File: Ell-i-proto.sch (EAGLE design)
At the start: 139 parts, among them J1 FTDI-SER-6, J10 PJ-102AX, J2 PWMH, J3 PWR, J4 PWML, J5 ANAL, J6 SPI, J7 COMM, J8 ANAH, J9 RJ45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

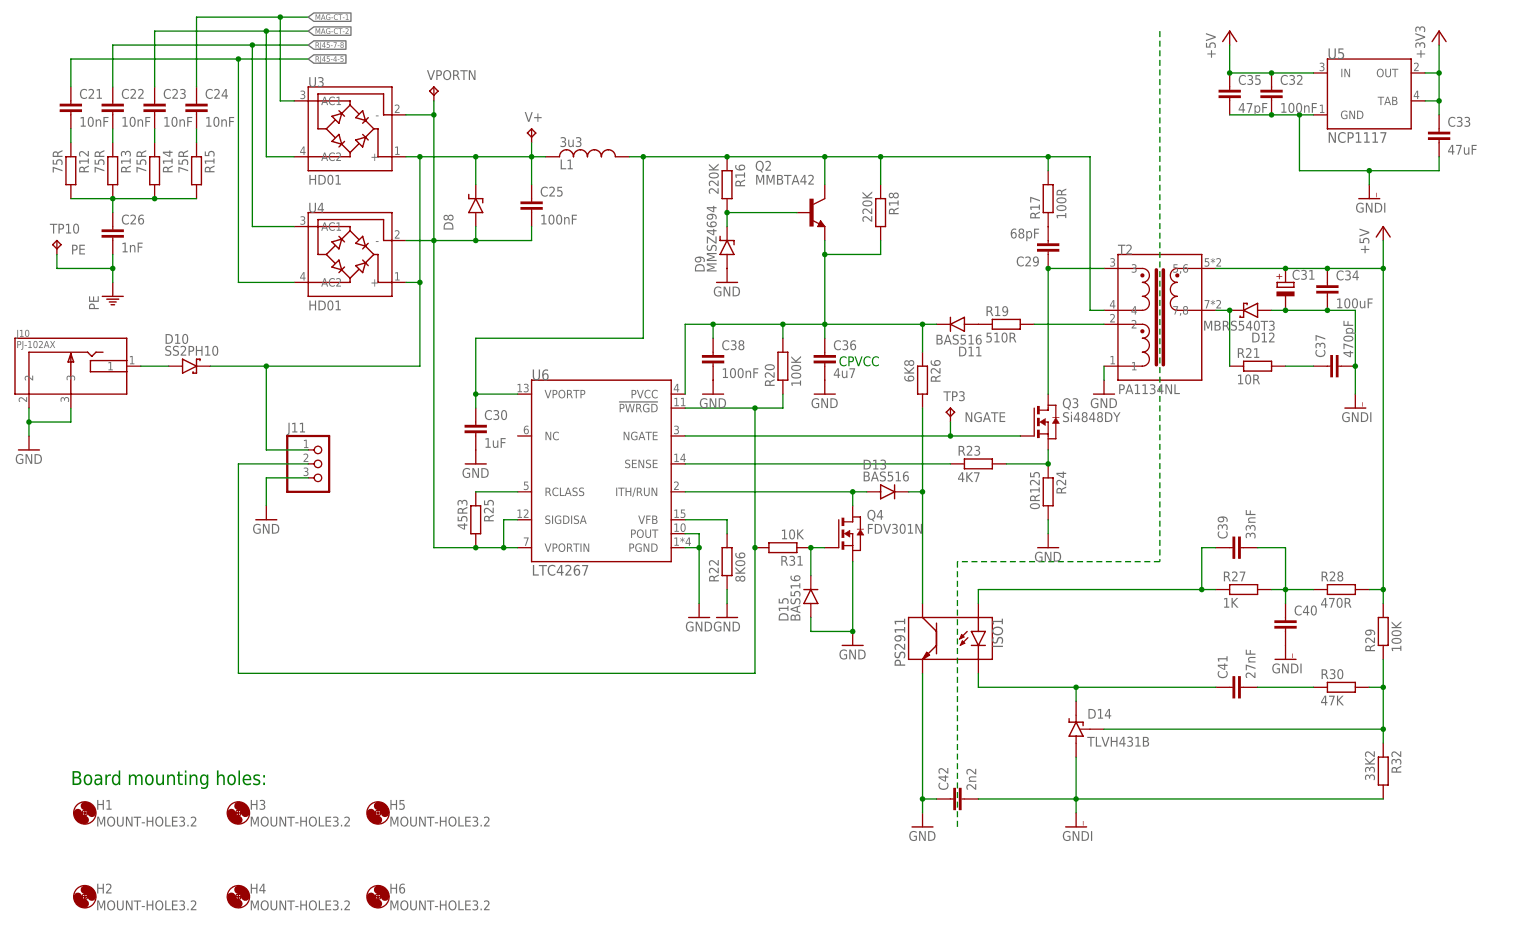
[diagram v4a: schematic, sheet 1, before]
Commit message: pushbutton and power LED to the right edge, some more drafting
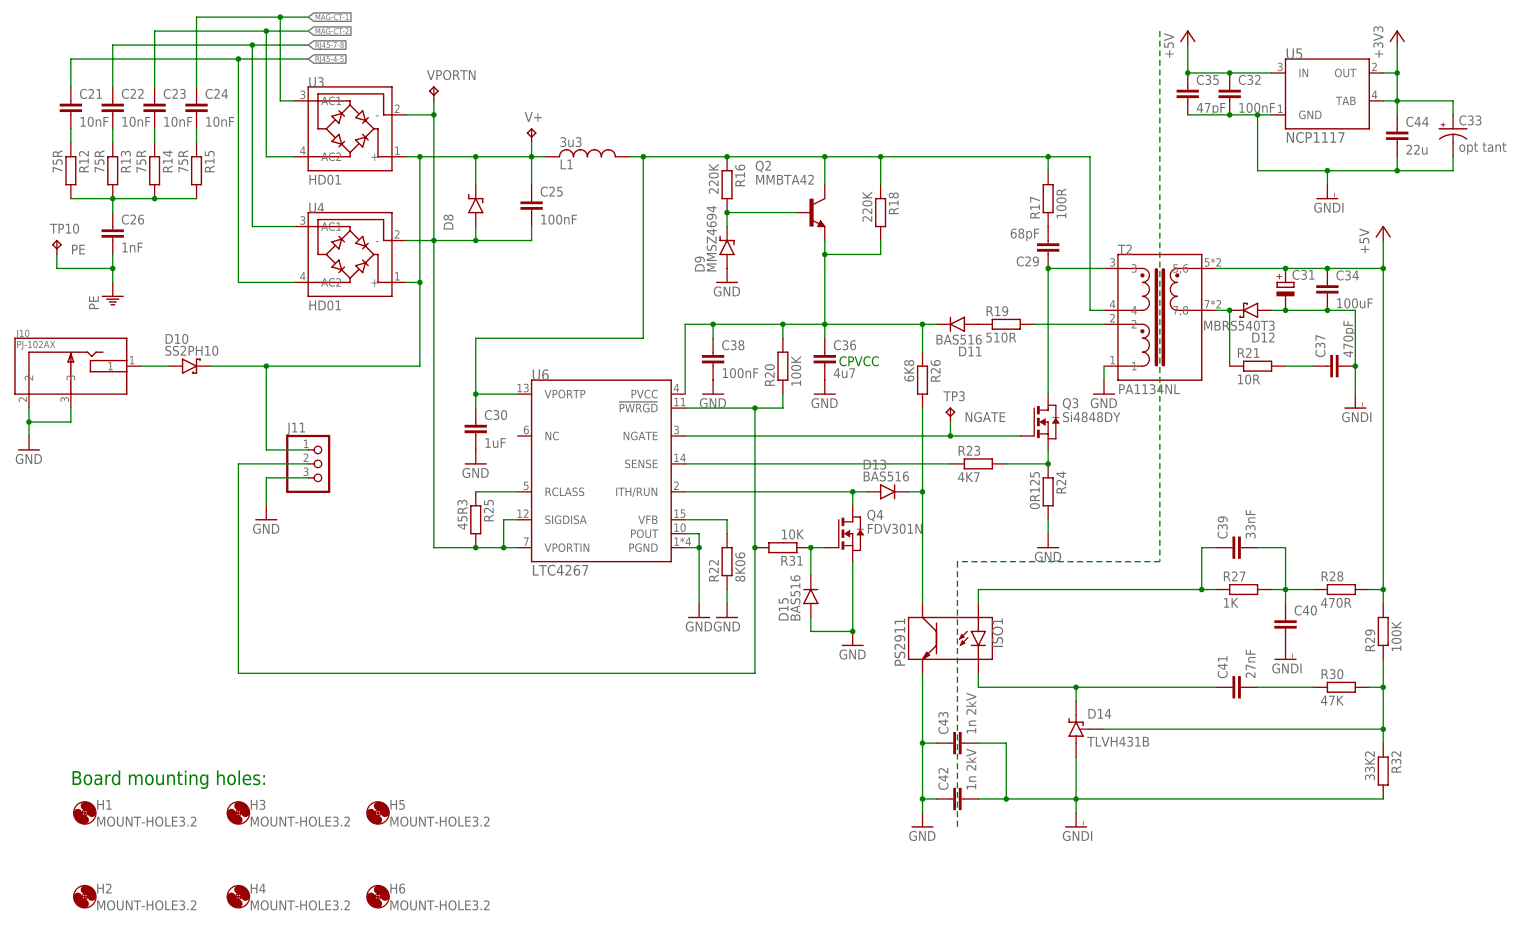
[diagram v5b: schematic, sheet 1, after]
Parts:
- added C43: 1n 2kV, rcl:C-EUC1206
- added C44: 22u, ell-i:C0805
- C33: value 47uF -> opt tant; device rcl:C-EUC1206 -> rcl:CPOL-USCT3216
- C42: value 2n2 -> 1n 2kV; device rcl:C-EUC1812 -> rcl:C-EUC1206
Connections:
- net +3V3: now also C33.+, C44.1; no longer C33.1
- net GND: now also C43.1
- net GNDI: now also C33.-, C43.2, C44.2; no longer C33.2
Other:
- moved on the sheet: C32, C35, U5
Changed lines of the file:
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@@
 <part name="C30" library="rcl" deviceset="C-EU" device="C1210" value="1uF"/>
 <part name="C32" library="ell-i" deviceset="C" device="0402" value="100nF"/>
-<part name="C33" library="rcl" deviceset="C-EU" device="C1206" value="47uF"/>
+<part name="C33" library="rcl" deviceset="CPOL-US" device="CT3216" value="opt tant"/>
 <part name="C34" library="rcl" deviceset="C-EU" device="C1206" value="100uF"/>
 <part name="C35" library="ell-i" deviceset="C" device="0402" value="47pF"/>
@@
 <part name="C39" library="ell-i" deviceset="C" device="0402" value="33nF"/>
 <part name="C41" library="ell-i" deviceset="C" device="0402" value="27nF"/>
-<part name="C42" library="rcl" deviceset="C-EU" device="C1812" value="2n2"/>
+<part name="C42" library="rcl" deviceset="C-EU" device="C1206" value="1n 2kV"/>
 <part name="D2" library="ell-i" deviceset="LED0603" device="" value="GRN"/>
 <part name="D4" library="ell-i" deviceset="LED0603" device="" value="STATUS"/>
@@
 <part name="S1" library="ell-i" deviceset="B3SL-10X2P" device=""/>
 <part name="J11" library="pinhead" deviceset="PINHD-1X3" device=""/>
+<part name="C44" library="ell-i" deviceset="C" device="0805" value="22u"/>
+<part name="C43" library="rcl" deviceset="C-EU" device="C1206" value="1n 2kV"/>
 </parts>
 <sheets>
@@
 <instance part="C29" gate="G$1" x="193.04" y="129.54" rot="R180"/>
 <instance part="C30" gate="G$1" x="88.9" y="99.06"/>
-<instance part="C32" gate="G$1" x="233.68" y="160.02"/>
-<instance part="C33" gate="G$1" x="264.16" y="152.4"/>
+<instance part="C32" gate="G$1" x="226.06" y="160.02"/>
+<instance part="C33" gate="G$1" x="266.7" y="152.4"/>
 <instance part="C34" gate="G$1" x="243.84" y="124.46"/>
-<instance part="C35" gate="G$1" x="226.06" y="160.02"/>
+<instance part="C35" gate="G$1" x="218.44" y="160.02"/>
 <instance part="C36" gate="G$1" x="152.4" y="111.76"/>
 <instance part="C37" gate="G$1" x="243.84" y="109.22" rot="R90"/>
@@
 <instance part="U3" gate="G$1" x="66.04" y="152.4"/>
 <instance part="U4" gate="G$1" x="66.04" y="129.54"/>
-<instance part="U5" gate="G$1" x="251.46" y="160.02"/>
+<instance part="U5" gate="G$1" x="243.84" y="160.02"/>
 <instance part="U6" gate="G$1" x="111.76" y="91.44"/>
 <instance part="D8" gate="G$1" x="88.9" y="139.7" rot="R90"/>
 <instance part="D9" gate="G$1" x="134.62" y="132.08" rot="R90"/>
-<instance part="+3V1" gate="G$1" x="264.16" y="170.18"/>
+<instance part="+3V1" gate="G$1" x="256.54" y="170.18"/>
 <instance part="GND13" gate="1" x="203.2" y="104.14"/>
 <instance part="GND14" gate="1" x="152.4" y="104.14"/>
@@
 <instance part="GND24" gate="1" x="7.62" y="93.98"/>
 <instance part="GNDI4" gate="G$1" x="198.12" y="25.4"/>
-<instance part="GNDI9" gate="G$1" x="251.46" y="139.7"/>
+<instance part="GNDI9" gate="G$1" x="243.84" y="139.7"/>
 <instance part="L1" gate="G$1" x="109.22" y="147.32"/>
 <instance part="P+3" gate="1" x="254" y="134.62"/>
@@
 <instance part="U$3" gate="G$1" x="0" y="0"/>
 <instance part="GNDI26" gate="G$1" x="248.92" y="101.6"/>
-<instance part="P+4" gate="1" x="226.06" y="170.18"/>
+<instance part="P+4" gate="1" x="218.44" y="170.18"/>
 <instance part="D10" gate="G$1" x="38.1" y="109.22"/>
 <instance part="TP3" gate="G$1" x="175.26" y="101.6"/>
@@
 <instance part="H6" gate="G$1" x="71.12" y="12.7"/>
 <instance part="J11" gate="A" x="60.96" y="91.44"/>
+<instance part="C44" gate="G$1" x="256.54" y="152.4"/>
+<instance part="C43" gate="G$1" x="175.26" y="40.64" rot="R90"/>
 </instances>
 <busses>
@@
 <pinref part="C42" gate="G$1" pin="1"/>
 <pinref part="ISO1" gate="G$1" pin="3"/>
-<wire x1="170.18" y1="53.34" x2="170.18" y2="30.48" width="0.1524" layer="91"/>
+<wire x1="170.18" y1="53.34" x2="170.18" y2="40.64" width="0.1524" layer="91"/>
+<wire x1="170.18" y1="40.64" x2="170.18" y2="30.48" width="0.1524" layer="91"/>
 <wire x1="170.18" y1="30.48" x2="170.18" y2="27.94" width="0.1524" layer="91"/>
 <pinref part="GND18" gate="1" pin="GND"/>
 <wire x1="172.72" y1="30.48" x2="170.18" y2="30.48" width="0.1524" layer="91"/>
 <junction x="170.18" y="30.48"/>
+<pinref part="C43" gate="G$1" pin="1"/>
+<wire x1="172.72" y1="40.64" x2="170.18" y2="40.64" width="0.1524" layer="91"/>
+<junction x="170.18" y="40.64"/>
 </segment>
 <segment>
@@
 <segment>
 <pinref part="U5" gate="G$1" pin="TAB"/>
-<pinref part="C33" gate="G$1" pin="1"/>
+<pinref part="C33" gate="G$1" pin="+"/>
 <pinref part="+3V1" gate="G$1" pin="+3V3"/>
-<wire x1="264.16" y1="167.64" x2="264.16" y2="162.56" width="0.1524" layer="91"/>
+<wire x1="256.54" y1="167.64" x2="256.54" y2="162.56" width="0.1524" layer="91"/>
 <pinref part="U5" gate="G$1" pin="OUT"/>
-<wire x1="264.16" y1="162.56" x2="264.16" y2="157.48" width="0.1524" layer="91"/>
-<wire x1="264.16" y1="157.48" x2="264.16" y2="154.94" width="0.1524" layer="91"/>
-<junction x="264.16" y="162.56"/>
-<wire x1="261.62" y1="162.56" x2="264.16" y2="162.56" width="0.1524" layer="91"/>
-<wire x1="261.62" y1="157.48" x2="264.16" y2="157.48" width="0.1524" layer="91"/>
-<junction x="264.16" y="157.48"/>
+<wire x1="256.54" y1="162.56" x2="256.54" y2="157.48" width="0.1524" layer="91"/>
+<wire x1="256.54" y1="157.48" x2="266.7" y2="157.48" width="0.1524" layer="91"/>
+<wire x1="266.7" y1="157.48" x2="266.7" y2="154.94" width="0.1524" layer="91"/>
+<junction x="256.54" y="162.56"/>
+<wire x1="254" y1="162.56" x2="256.54" y2="162.56" width="0.1524" layer="91"/>
+<wire x1="254" y1="157.48" x2="256.54" y2="157.48" width="0.1524" layer="91"/>
+<junction x="256.54" y="157.48"/>
+<pinref part="C44" gate="G$1" pin="1"/>
+<wire x1="256.54" y1="154.94" x2="256.54" y2="157.48" width="0.1524" layer="91"/>
 </segment>
 </net>
@@
 <pinref part="C42" gate="G$1" pin="2"/>
 <wire x1="198.12" y1="30.48" x2="198.12" y2="38.1" width="0.1524" layer="91"/>
-<wire x1="180.34" y1="30.48" x2="198.12" y2="30.48" width="0.1524" layer="91"/>
+<wire x1="180.34" y1="30.48" x2="185.42" y2="30.48" width="0.1524" layer="91"/>
 <junction x="198.12" y="30.48"/>
+<wire x1="185.42" y1="30.48" x2="198.12" y2="30.48" width="0.1524" layer="91"/>
 <wire x1="198.12" y1="30.48" x2="254" y2="30.48" width="0.1524" layer="91"/>
+<wire x1="185.42" y1="30.48" x2="185.42" y2="40.64" width="0.1524" layer="91"/>
+<pinref part="C43" gate="G$1" pin="2"/>
+<wire x1="185.42" y1="40.64" x2="180.34" y2="40.64" width="0.1524" layer="91"/>
+<junction x="185.42" y="30.48"/>
 </segment>
 <segment>
@@
 <pinref part="C35" gate="G$1" pin="2"/>
 <pinref part="C32" gate="G$1" pin="2"/>
-<wire x1="226.06" y1="154.94" x2="233.68" y2="154.94" width="0.1524" layer="91"/>
+<wire x1="218.44" y1="154.94" x2="226.06" y2="154.94" width="0.1524" layer="91"/>
 <pinref part="U5" gate="G$1" pin="GND"/>
-<wire x1="233.68" y1="154.94" x2="238.76" y2="154.94" width="0.1524" layer="91"/>
-<pinref part="C33" gate="G$1" pin="2"/>
-<wire x1="238.76" y1="154.94" x2="241.3" y2="154.94" width="0.1524" layer="91"/>
-<wire x1="251.46" y1="142.24" x2="251.46" y2="144.78" width="0.1524" layer="91"/>
-<wire x1="251.46" y1="144.78" x2="264.16" y2="144.78" width="0.1524" layer="91"/>
-<wire x1="264.16" y1="144.78" x2="264.16" y2="147.32" width="0.1524" layer="91"/>
+<wire x1="226.06" y1="154.94" x2="231.14" y2="154.94" width="0.1524" layer="91"/>
+<pinref part="C33" gate="G$1" pin="-"/>
+<wire x1="231.14" y1="154.94" x2="233.68" y2="154.94" width="0.1524" layer="91"/>
+<wire x1="243.84" y1="142.24" x2="243.84" y2="144.78" width="0.1524" layer="91"/>
+<wire x1="243.84" y1="144.78" x2="256.54" y2="144.78" width="0.1524" layer="91"/>
+<wire x1="256.54" y1="144.78" x2="266.7" y2="144.78" width="0.1524" layer="91"/>
+<wire x1="266.7" y1="144.78" x2="266.7" y2="147.32" width="0.1524" layer="91"/>
 <pinref part="GNDI9" gate="G$1" pin="GNDI"/>
-<junction x="233.68" y="154.94"/>
-<wire x1="238.76" y1="144.78" x2="238.76" y2="154.94" width="0.1524" layer="91"/>
-<junction x="238.76" y="154.94"/>
-<wire x1="251.46" y1="144.78" x2="238.76" y2="144.78" width="0.1524" layer="91"/>
-<junction x="251.46" y="144.78"/>
+<junction x="226.06" y="154.94"/>
+<wire x1="231.14" y1="144.78" x2="231.14" y2="154.94" width="0.1524" layer="91"/>
+<junction x="231.14" y="154.94"/>
+<wire x1="243.84" y1="144.78" x2="231.14" y2="144.78" width="0.1524" layer="91"/>
+<junction x="243.84" y="144.78"/>
+<pinref part="C44" gate="G$1" pin="2"/>
+<wire x1="256.54" y1="144.78" x2="256.54" y2="147.32" width="0.1524" layer="91"/>
+<junction x="256.54" y="144.78"/>
 </segment>
 <segment>
@@
 <pinref part="U5" gate="G$1" pin="IN"/>
 <pinref part="C32" gate="G$1" pin="1"/>
-<wire x1="233.68" y1="162.56" x2="241.3" y2="162.56" width="0.1524" layer="91"/>
-<junction x="233.68" y="162.56"/>
-<pinref part="C35" gate="G$1" pin="1"/>
 <wire x1="226.06" y1="162.56" x2="233.68" y2="162.56" width="0.1524" layer="91"/>
 <junction x="226.06" y="162.56"/>
+<pinref part="C35" gate="G$1" pin="1"/>
+<wire x1="218.44" y1="162.56" x2="226.06" y2="162.56" width="0.1524" layer="91"/>
+<junction x="218.44" y="162.56"/>
 <pinref part="P+4" gate="1" pin="+5V"/>
-<wire x1="226.06" y1="167.64" x2="226.06" y2="162.56" width="0.1524" layer="91"/>
-</segment>
-<segment>
+<wire x1="218.44" y1="167.64" x2="218.44" y2="162.56" width="0.1524" layer="91"/>
+</segment>
+<segment>

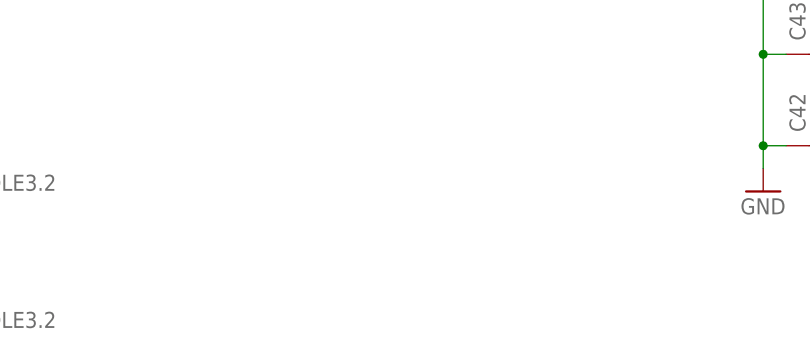
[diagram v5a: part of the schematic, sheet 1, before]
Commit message: component placement closer to reality..
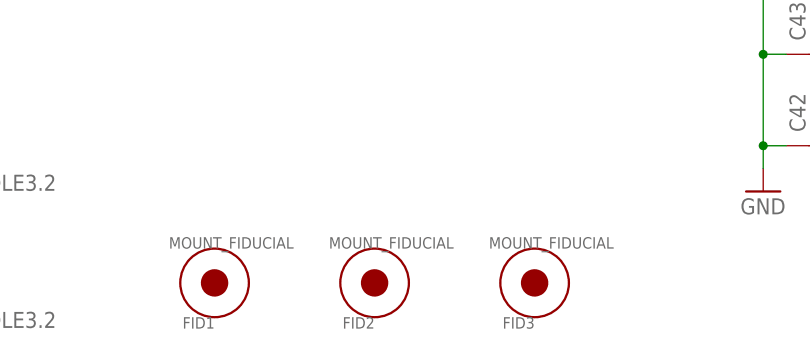
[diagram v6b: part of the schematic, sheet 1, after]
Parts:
- added FID1, FID2, FID3: MOUNT_FIDUCIAL, ell-i:MOUNT_FIDUCIAL
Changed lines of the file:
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@@
 <part name="C44" library="ell-i" deviceset="C" device="0805" value="22u"/>
 <part name="C43" library="rcl" deviceset="C-EU" device="C1206" value="1n 2kV"/>
+<part name="FID1" library="ell-i" deviceset="MOUNT_FIDUCIAL" device=""/>
+<part name="FID2" library="ell-i" deviceset="MOUNT_FIDUCIAL" device=""/>
+<part name="FID3" library="ell-i" deviceset="MOUNT_FIDUCIAL" device=""/>
 </parts>
 <sheets>
@@
 <instance part="C44" gate="G$1" x="256.54" y="152.4"/>
 <instance part="C43" gate="G$1" x="175.26" y="40.64" rot="R90"/>
+<instance part="FID1" gate="G$1" x="109.22" y="15.24"/>
+<instance part="FID2" gate="G$1" x="127" y="15.24"/>
+<instance part="FID3" gate="G$1" x="144.78" y="15.24"/>
 </instances>
 <busses>
